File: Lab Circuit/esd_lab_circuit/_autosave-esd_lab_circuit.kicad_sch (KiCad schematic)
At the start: 5 parts, among them U3 74LS373, U5 ATF16V8Bxx-xxPU, U6 M48Z35

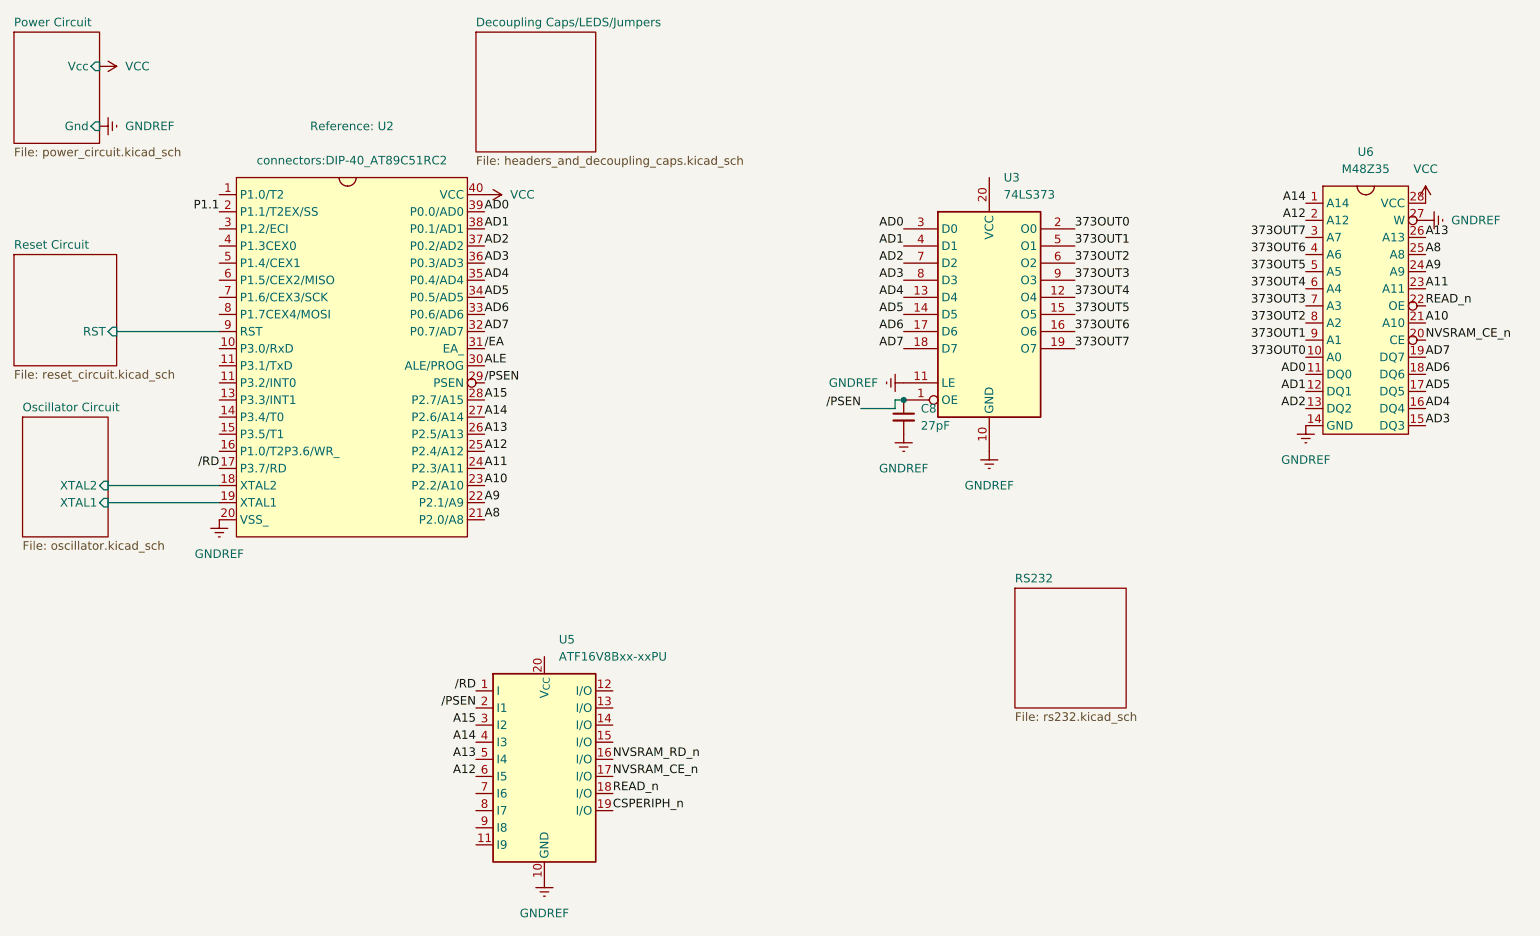
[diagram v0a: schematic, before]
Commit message: Fixed the timer
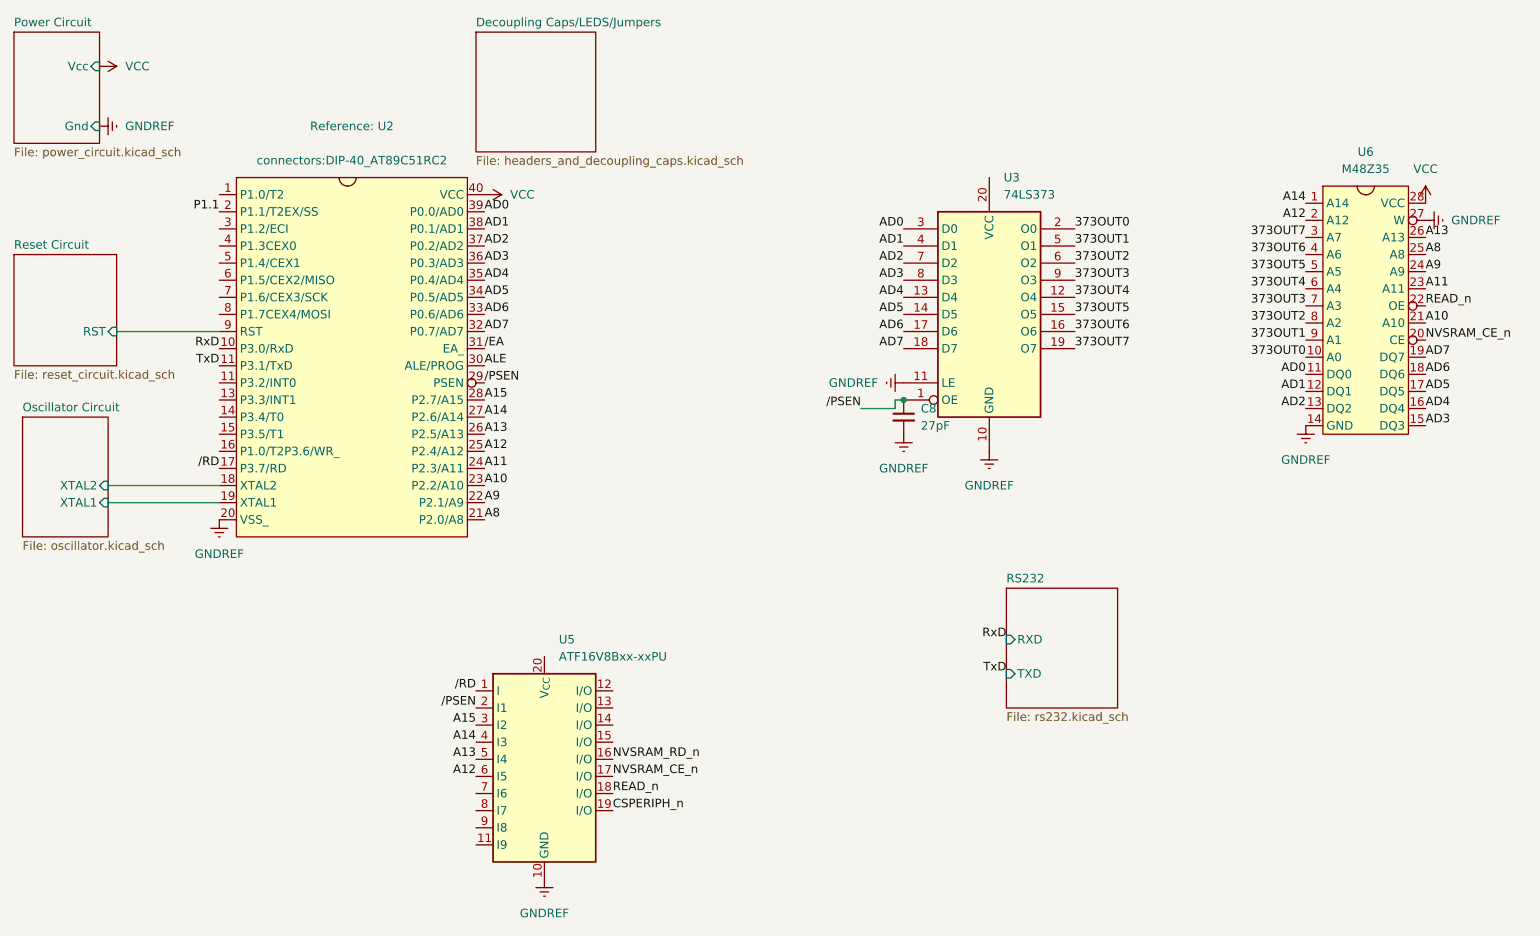
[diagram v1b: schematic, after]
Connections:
- net RxD: now reaches U2.10 (P3.0/RxD)
- net TxD: now reaches U2.11 (P3.2/INT0)
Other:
- sheet RS232 ports: added RXD, TXD; removed none
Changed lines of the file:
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@@
+		)
+	)
+	(label "TxD"
+		(at 161.29 110.49 180)
+		(effects
+			(font
+				(size 1.27 1.27)
+			)
+			(justify right bottom)
 		)
 	)
@@
 		)
 	)
+	(label "RxD"
+		(at 161.29 105.41 180)
+		(effects
+			(font
+				(size 1.27 1.27)
+			)
+			(justify right bottom)
+		)
+	)
 	(label "A10"
 		(at 83.82 82.55 0)
@@
 		)
 	)
+	(label "RxD"
+		(at 44.45 62.23 180)
+		(effects
+			(font
+				(size 1.27 1.27)
+			)
+			(justify right bottom)
+		)
+	)
 	(label "373OUT4"
 		(at 171.45 54.61 0)
@@
 	(label "/PSEN"
 		(at 82.55 115.57 180)
+		(effects
+			(font
+				(size 1.27 1.27)
+			)
+			(justify right bottom)
+		)
+	)
+	(label "TxD"
+		(at 44.45 64.77 180)
 		(effects
 			(font
@@
 	)
 	(sheet
-		(at 162.56 97.79)
+		(at 161.29 97.79)
 		(size 16.51 17.78)
 		(exclude_from_sim no)
@@
 		)
 		(property "Sheetname" "RS232"
-			(at 162.56 97.0784 0)
+			(at 161.29 97.0784 0)
 			(effects
 				(font
@@
 		)
 		(property "Sheetfile" "rs232.kicad_sch"
-			(at 162.56 116.1546 0)
+			(at 161.29 116.1546 0)
 			(effects
 				(font
@@
 			)
 		)
+		(pin "RXD" input
+			(at 161.29 105.41 180)
+			(effects
+				(font
+					(size 1.27 1.27)
+				)
+				(justify left)
+			)
+		)
+		(pin "TXD" input
+			(at 161.29 110.49 180)
+			(effects
+				(font
+					(size 1.27 1.27)
+				)
+				(justify left)
+			)
+		)
